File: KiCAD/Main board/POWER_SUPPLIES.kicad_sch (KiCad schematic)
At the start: 1 part, among them U18 12V

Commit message: Worked on KiCAD
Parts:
- added U19: 5V, Audio-DSP:BUCK_MAX17634C, symbol Audio_DSP:BUCK_5V_MAX17634C
- added U20: 8V, Audio-DSP:BUCK_MAX17634C, symbol Audio_DSP:BUCK_8V_MAX17634C
- added U21: 15V, Audio-DSP:BUCK_MAX17634C, symbol Audio_DSP:BUCK_15V_MAX17634C
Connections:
- net GND: now also U19.2 (GND), U20.2 (GND), U21.2 (GND)
- net at U18.3 (VIN): now also U19.3 (VIN), U20.3 (VIN), U21.3 (VIN)
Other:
- moved on the sheet: U18
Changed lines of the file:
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@@
 (kicad_sch (version 20230121) (generator eeschema)
   (paper "A4")
-  (wire (pts (xy 123.19 52.07) (xy 123.19 53.34))
-    (stroke (width 0) (type default))
-  )
-  (symbol (lib_id "power:GND") (at 123.19 53.34 0) (unit 1)
-    (in_bom yes) (on_board yes) (dnp no) (fields_autoplaced)
-    (property "Reference" "#PWR097" (at 123.19 59.69 0)
-      (effects (font (size 1.27 1.27)) hide)
-    )
-    (property "Value" "GND" (at 123.19 58.42 0)
-      (effects (font (size 1.27 1.27)))
-    )
-    (property "Footprint" "" (at 123.19 53.34 0)
-      (effects (font (size 1.27 1.27)) hide)
-    )
-    (property "Datasheet" "" (at 123.19 53.34 0)
+  (junction (at 110.49 93.98) (diameter 0) (color 0 0 0 0)
+  )
+  (junction (at 110.49 40.64) (diameter 0) (color 0 0 0 0)
+  )
+  (junction (at 110.49 67.31) (diameter 0) (color 0 0 0 0)
+  )
+  (wire (pts (xy 110.49 40.64) (xy 110.49 67.31))
+    (stroke (width 0) (type default))
+  )
+  (wire (pts (xy 121.92 77.47) (xy 121.92 78.74))
+    (stroke (width 0) (type default))
+  )
+  (wire (pts (xy 121.92 130.81) (xy 121.92 132.08))
+    (stroke (width 0) (type default))
+  )
+  (wire (pts (xy 110.49 67.31) (xy 110.49 93.98))
+    (stroke (width 0) (type default))
+  )
+  (wire (pts (xy 110.49 93.98) (xy 110.49 120.65))
+    (stroke (width 0) (type default))
+  )
+  (wire (pts (xy 121.92 104.14) (xy 121.92 105.41))
+    (stroke (width 0) (type default))
+  )
+  (wire (pts (xy 106.68 40.64) (xy 110.49 40.64))
+    (stroke (width 0) (type default))
+  )
+  (wire (pts (xy 121.92 50.8) (xy 121.92 52.07))
+    (stroke (width 0) (type default))
+  )
+  (symbol (lib_id "power:GND") (at 121.92 132.08 0) (unit 1)
+    (in_bom yes) (on_board yes) (dnp no) (fields_autoplaced)
+    (property "Reference" "#PWR098" (at 121.92 138.43 0)
+      (effects (font (size 1.27 1.27)) hide)
+    )
+    (property "Value" "GND" (at 121.92 137.16 0)
+      (effects (font (size 1.27 1.27)))
+    )
+    (property "Footprint" "" (at 121.92 132.08 0)
+      (effects (font (size 1.27 1.27)) hide)
+    )
+    (property "Datasheet" "" (at 121.92 132.08 0)
+      (effects (font (size 1.27 1.27)) hide)
+    )
+    (pin "1")
+    (instances
+      (project "Main board"
+        (path "/2f8cbac6-fd11-4240-8e40-3bb6952a0324/fc272ee1-9060-465b-85c1-b8364d68deb3"
+          (reference "#PWR098") (unit 1)
+        )
+      )
+    )
+  )
+  (symbol (lib_id "Audio_DSP:BUCK_5V_MAX17634C") (at 121.92 41.91 0) (unit 1)
+    (in_bom yes) (on_board yes) (dnp no) (fields_autoplaced)
+    (property "Reference" "U19" (at 121.92 34.29 0)
+      (effects (font (size 1.27 1.27)))
+    )
+    (property "Value" "5V" (at 121.92 36.83 0)
+      (effects (font (size 1.27 1.27)))
+    )
+    (property "Footprint" "Audio-DSP:BUCK_MAX17634C" (at 121.92 41.91 0)
+      (effects (font (size 1.27 1.27)) hide)
+    )
+    (property "Datasheet" "NA" (at 121.92 41.91 0)
+      (effects (font (size 1.27 1.27)) hide)
+    )
+    (pin "1")
+    (pin "2")
+    (pin "3")
+    (instances
+      (project "Main board"
+        (path "/2f8cbac6-fd11-4240-8e40-3bb6952a0324/fc272ee1-9060-465b-85c1-b8364d68deb3"
+          (reference "U19") (unit 1)
+        )
+      )
+    )
+  )
+  (symbol (lib_id "power:GND") (at 121.92 52.07 0) (unit 1)
+    (in_bom yes) (on_board yes) (dnp no) (fields_autoplaced)
+    (property "Reference" "#PWR0100" (at 121.92 58.42 0)
+      (effects (font (size 1.27 1.27)) hide)
+    )
+    (property "Value" "GND" (at 121.92 57.15 0)
+      (effects (font (size 1.27 1.27)))
+    )
+    (property "Footprint" "" (at 121.92 52.07 0)
+      (effects (font (size 1.27 1.27)) hide)
+    )
+    (property "Datasheet" "" (at 121.92 52.07 0)
+      (effects (font (size 1.27 1.27)) hide)
+    )
+    (pin "1")
+    (instances
+      (project "Main board"
+        (path "/2f8cbac6-fd11-4240-8e40-3bb6952a0324/fc272ee1-9060-465b-85c1-b8364d68deb3"
+          (reference "#PWR0100") (unit 1)
+        )
+      )
+    )
+  )
+  (symbol (lib_id "Audio_DSP:BUCK_8V_MAX17634C") (at 121.92 68.58 0) (unit 1)
+    (in_bom yes) (on_board yes) (dnp no) (fields_autoplaced)
+    (property "Reference" "U20" (at 121.92 60.96 0)
+      (effects (font (size 1.27 1.27)))
+    )
+    (property "Value" "8V" (at 121.92 63.5 0)
+      (effects (font (size 1.27 1.27)))
+    )
+    (property "Footprint" "Audio-DSP:BUCK_MAX17634C" (at 121.92 68.58 0)
+      (effects (font (size 1.27 1.27)) hide)
+    )
+    (property "Datasheet" "NA" (at 121.92 68.58 0)
+      (effects (font (size 1.27 1.27)) hide)
+    )
+    (pin "1")
+    (pin "2")
+    (pin "3")
+    (instances
+      (project "Main board"
+        (path "/2f8cbac6-fd11-4240-8e40-3bb6952a0324/fc272ee1-9060-465b-85c1-b8364d68deb3"
+          (reference "U20") (unit 1)
+        )
+      )
+    )
+  )
+  (symbol (lib_id "power:GND") (at 121.92 105.41 0) (unit 1)
+    (in_bom yes) (on_board yes) (dnp no) (fields_autoplaced)
+    (property "Reference" "#PWR097" (at 121.92 111.76 0)
+      (effects (font (size 1.27 1.27)) hide)
+    )
+    (property "Value" "GND" (at 121.92 110.49 0)
+      (effects (font (size 1.27 1.27)))
+    )
+    (property "Footprint" "" (at 121.92 105.41 0)
+      (effects (font (size 1.27 1.27)) hide)
+    )
+    (property "Datasheet" "" (at 121.92 105.41 0)
       (effects (font (size 1.27 1.27)) hide)
     )
@@
     )
   )
-  (symbol (lib_id "Audio_DSP:BUCK_12V_MAX17634C") (at 123.19 43.18 0) (unit 1)
-    (in_bom yes) (on_board yes) (dnp no) (fields_autoplaced)
-    (property "Reference" "U18" (at 123.19 35.56 0)
-      (effects (font (size 1.27 1.27)))
-    )
-    (property "Value" "12V" (at 123.19 38.1 0)
-      (effects (font (size 1.27 1.27)))
-    )
-    (property "Footprint" "Audio-DSP:BUCK_MAX17634C" (at 123.19 43.18 0)
-      (effects (font (size 1.27 1.27)) hide)
-    )
-    (property "Datasheet" "NA" (at 123.19 43.18 0)
+  (symbol (lib_id "Audio_DSP:BUCK_12V_MAX17634C") (at 121.92 95.25 0) (unit 1)
+    (in_bom yes) (on_board yes) (dnp no) (fields_autoplaced)
+    (property "Reference" "U18" (at 121.92 87.63 0)
+      (effects (font (size 1.27 1.27)))
+    )
+    (property "Value" "12V" (at 121.92 90.17 0)
+      (effects (font (size 1.27 1.27)))
+    )
+    (property "Footprint" "Audio-DSP:BUCK_MAX17634C" (at 121.92 95.25 0)
+      (effects (font (size 1.27 1.27)) hide)
+    )
+    (property "Datasheet" "NA" (at 121.92 95.25 0)
       (effects (font (size 1.27 1.27)) hide)
     )
@@
         )
       )
+    )
+  )
+  (symbol (lib_id "Audio_DSP:BUCK_15V_MAX17634C") (at 121.92 121.92 0) (unit 1)
+    (in_bom yes) (on_board yes) (dnp no) (fields_autoplaced)
+    (property "Reference" "U21" (at 121.92 114.3 0)
+      (effects (font (size 1.27 1.27)))
+    )
+    (property "Value" "15V" (at 121.92 116.84 0)
+      (effects (font (size 1.27 1.27)))
+    )
+    (property "Footprint" "Audio-DSP:BUCK_MAX17634C" (at 121.92 121.92 0)
+      (effects (font (size 1.27 1.27)) hide)
+    )
+    (property "Datasheet" "NA" (at 121.92 121.92 0)
+      (effects (font (size 1.27 1.27)) hide)
+    )
+    (pin "1")
+    (pin "2")
+    (pin "3")
+    (instances
+      (project "Main board"
+        (path "/2f8cbac6-fd11-4240-8e40-3bb6952a0324/fc272ee1-9060-465b-85c1-b8364d68deb3"
+          (reference "U21") (unit 1)
+        )
+      )
+    )
+  )
+  (symbol (lib_id "power:GND") (at 121.92 78.74 0) (unit 1)
+    (in_bom yes) (on_board yes) (dnp no) (fields_autoplaced)
+    (property "Reference" "#PWR099" (at 121.92 85.09 0)
+      (effects (font (size 1.27 1.27)) hide)
+    )
+    (property "Value" "GND" (at 121.92 83.82 0)
+      (effects (font (size 1.27 1.27)))
+    )
+    (property "Footprint" "" (at 121.92 78.74 0)
+      (effects (font (size 1.27 1.27)) hide)
+    )
+    (property "Datasheet" "" (at 121.92 78.74 0)
+      (effects (font (size 1.27 1.27)) hide)
+    )
+    (pin "1")
+    (instances
+      (project "Main board"
+        (path "/2f8cbac6-fd11-4240-8e40-3bb6952a0324/fc272ee1-9060-465b-85c1-b8364d68deb3"
+          (reference "#PWR099") (unit 1)
+        )
+      )

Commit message: Worked on the main board
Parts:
- added U23 (x2): LIN_REG_±5V, Audio_DSP:LIN_REG_±xxV, symbol Audio-DSP:LIN_REG_±5V
- added U24 (x2): LIN_REG_±12V, Audio_DSP:LIN_REG_±xxV, symbol Audio-DSP:LIN_REG_±12V
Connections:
- net GND: now also U23.2 (GND), U23.2 (GND), U23.5 (GND), U23.5 (GND), U24.2 (GND), U24.2 (GND), U24.5 (GND), U24.5 (GND)
- new net +12VA: U24.3 (+12V)
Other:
- note added: "1"
- note added: "2"

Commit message: Worked on main board
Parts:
- U18, U19, U20, U21: footprint Audio-DSP:BUCK_MAX17634C -> Audio-DSP:BUCK_MAX17634C_xxV
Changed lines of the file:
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@@
       (effects (font (size 1.27 1.27)))
     )
-    (property "Footprint" "Audio-DSP:BUCK_MAX17634C" (at 121.92 41.91 0)
+    (property "Footprint" "Audio-DSP:BUCK_MAX17634C_xxV" (at 121.92 41.91 0)
       (effects (font (size 1.27 1.27)) hide)
     )
@@
       (effects (font (size 1.27 1.27)))
     )
-    (property "Footprint" "Audio-DSP:BUCK_MAX17634C" (at 121.92 68.58 0)
+    (property "Footprint" "Audio-DSP:BUCK_MAX17634C_xxV" (at 121.92 68.58 0)
       (effects (font (size 1.27 1.27)) hide)
     )
@@
       (effects (font (size 1.27 1.27)))
     )
-    (property "Footprint" "Audio-DSP:BUCK_MAX17634C" (at 121.92 95.25 0)
+    (property "Footprint" "Audio-DSP:BUCK_MAX17634C_xxV" (at 121.92 95.25 0)
       (effects (font (size 1.27 1.27)) hide)
     )
@@
       (effects (font (size 1.27 1.27)))
     )
-    (property "Footprint" "Audio-DSP:BUCK_MAX17634C" (at 121.92 121.92 0)
-      (effects (font (size 1.27 1.27)) hide)
-    )
+    (property "Footprint" "Audio-DSP:BUCK_MAX17634C_xxV" (at 121.92 121.92 0)
+      (effects (font (size 1.27 1.27)) hide)
+    )

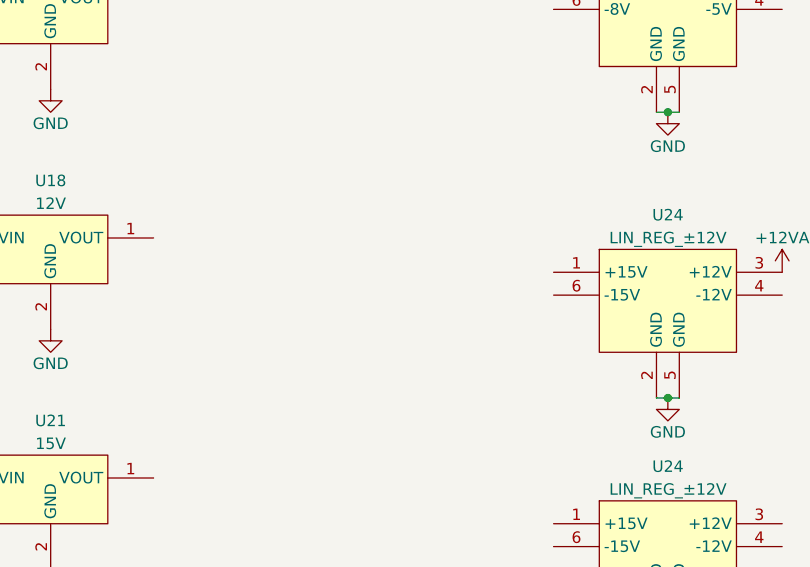
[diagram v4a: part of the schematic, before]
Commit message: Added SEPIC symbol and footprint and worked on main board
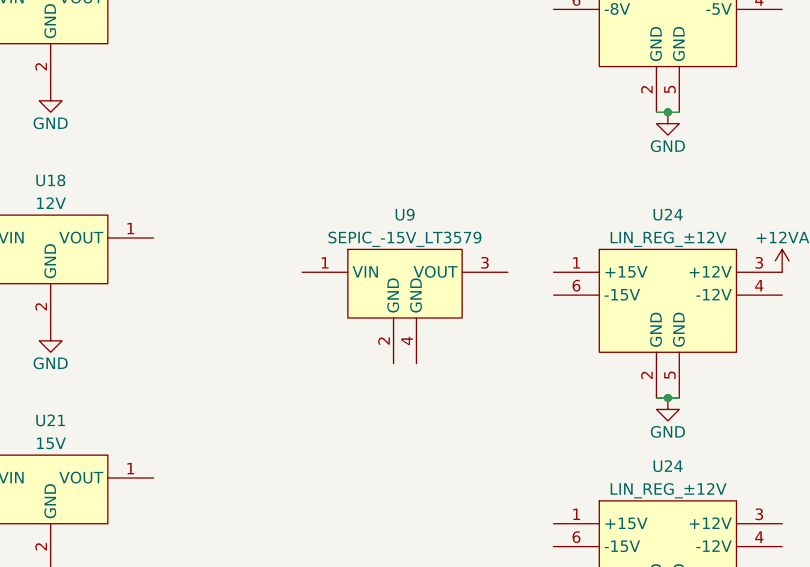
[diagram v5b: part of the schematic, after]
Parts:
- added U9: SEPIC_-15V_LT3579, Audio-DSP:SEPIC_-15V_LT3579, symbol Audio_DSP:SEPIC_-15V_LT3579
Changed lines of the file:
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@@
+    )
+  )
+  (symbol (lib_id "Audio_DSP:SEPIC_-15V_LT3579") (at 161.29 99.06 0) (unit 1)
+    (in_bom yes) (on_board yes) (dnp no) (fields_autoplaced)
+    (property "Reference" "U9" (at 161.29 91.44 0)
+      (effects (font (size 1.27 1.27)))
+    )
+    (property "Value" "SEPIC_-15V_LT3579" (at 161.29 93.98 0)
+      (effects (font (size 1.27 1.27)))
+    )
+    (property "Footprint" "Audio-DSP:SEPIC_-15V_LT3579" (at 161.29 99.06 0)
+      (effects (font (size 1.27 1.27)) hide)
+    )
+    (property "Datasheet" "NA" (at 161.29 99.06 0)
+      (effects (font (size 1.27 1.27)) hide)
+    )
+    (pin "1")
+    (pin "2")
+    (pin "3")
+    (pin "4")
+    (instances
+      (project "Main board"
+        (path "/2f8cbac6-fd11-4240-8e40-3bb6952a0324/fc272ee1-9060-465b-85c1-b8364d68deb3"
+          (reference "U9") (unit 1)
+        )
+      )
     )
   )
